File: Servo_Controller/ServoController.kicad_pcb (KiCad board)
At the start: 2 copper layers, 71.5 x 20.8 mm, 43 parts, among them J1 USB_B_Micro, K1 SWD, K2 Signal/Power, M1 Motor, U1 STM32F103C8T6, U2 TPD2E001DZDR, U3 AMS1117-3.3, U4 IRS4427S, U5 AO4616, U6 AO4616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

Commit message: Manufacturing data added
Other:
- board text added: "Servo controller"
- board text removed: "Servo controller - Variant {dblquote}A{dblquote}"
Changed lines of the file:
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@@
   (gr_line (start 304.25 191.75) (end 239.5 191.75) (layer "Edge.Cuts") (width 0.1))
   (gr_arc (start 239.5 212.5) (mid 239.146447 212.353553) (end 239 212) (layer "Edge.Cuts") (width 0.1))
-  (gr_text "Servo controller - Variant {dblquote}A{dblquote}" (at 278.3 208.25) (layer "B.SilkS")
+  (gr_text "Servo controller" (at 281.5 209.25) (layer "B.SilkS")
     (effects (font (size 1 1) (thickness 0.15)) (justify mirror))
   )

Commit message: Manual assembly PDF added, value/reference sizes changed in PCB
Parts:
- K1: value SWD -> *VAL
- renumbered R4 to Rw

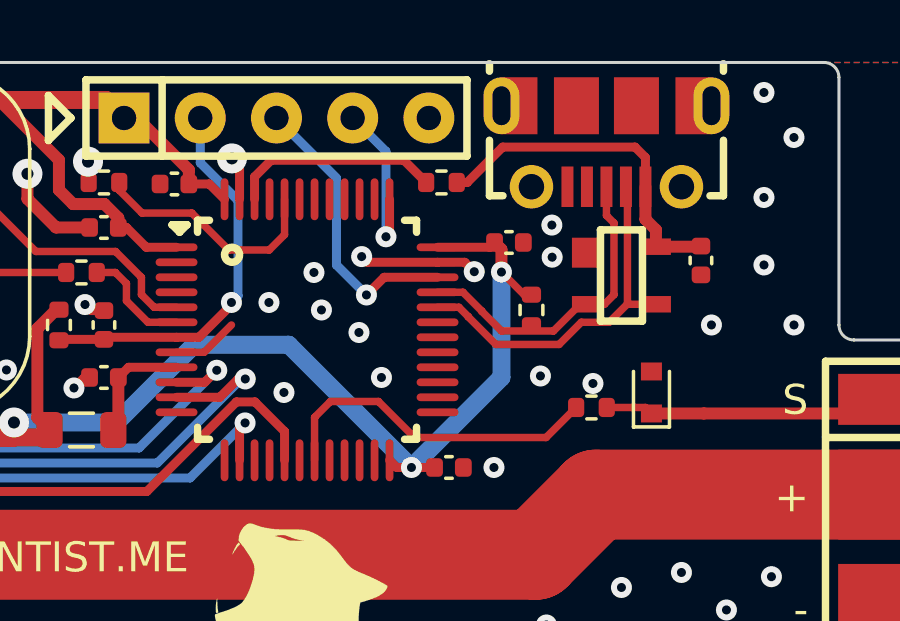
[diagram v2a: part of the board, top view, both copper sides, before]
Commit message: Added enclosure, removed unnecessary resistor
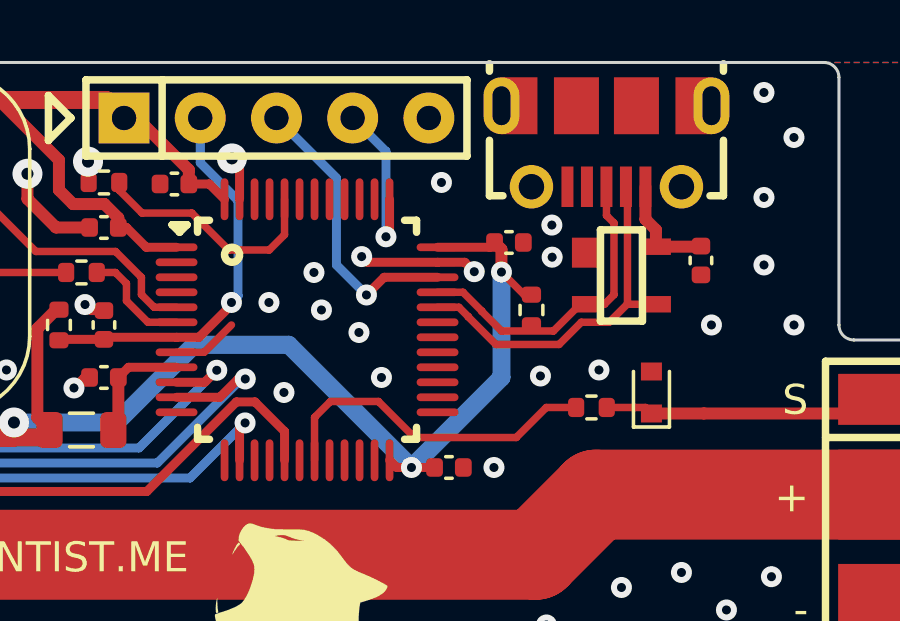
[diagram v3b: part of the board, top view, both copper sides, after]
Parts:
- removed R1: 4.7k, ServoController:R_0402
- removed Rw: 1k, ServoController:R_0402
- added R4: 1k, ServoController:R_0402, F.Cu at (296.5, 203.2)
- K1: value *VAL -> SWD
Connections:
- U1 pad 46: /USB_DET -> unconnected-(U1-Pad46)
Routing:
- net Net-(C1-Pad1): track 11.5 -> 3.65 mm
- net /USB_DET: track 7.00 -> 0.00 mm
- net GND: vias 79 -> 80

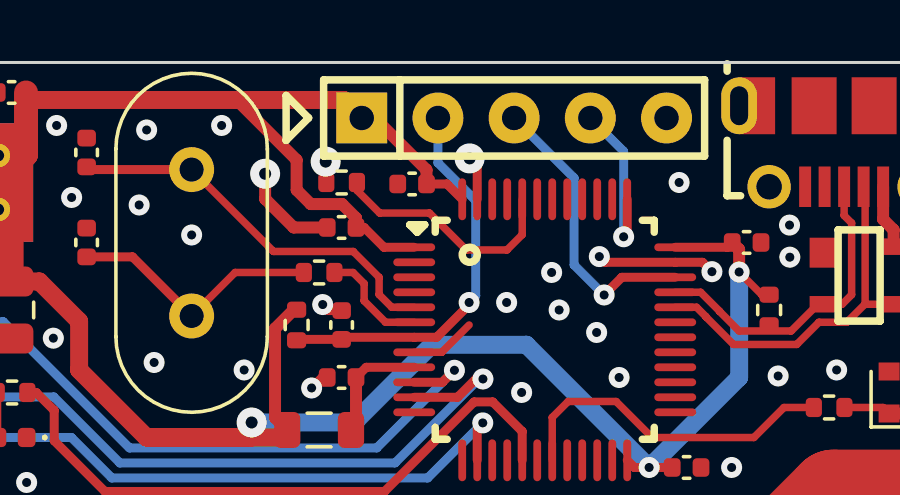
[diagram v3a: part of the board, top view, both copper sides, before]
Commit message: Changed VCC to SWO signal on SWD header. Manufacturing data and PCB previews updated
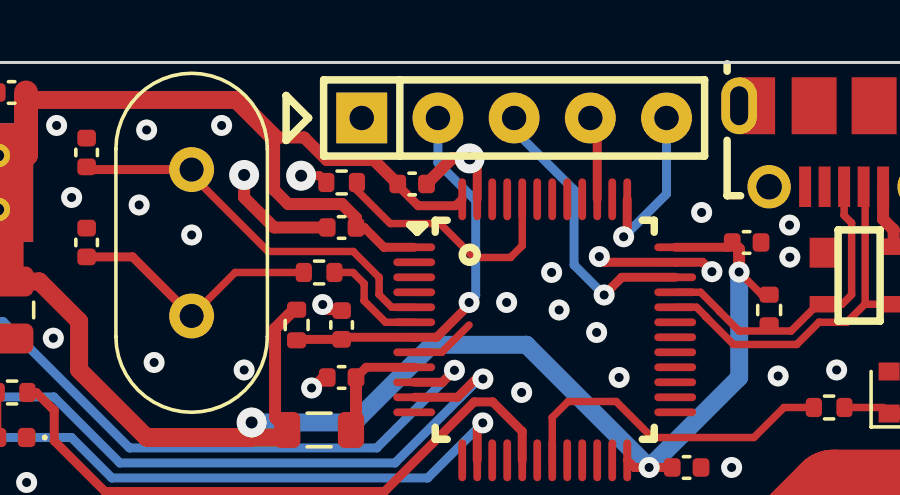
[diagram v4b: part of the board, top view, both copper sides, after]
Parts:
- turned C9 to 0 degrees
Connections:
- J1 pad 6: unconnected-(J1-Pad6) -> (no net)
- K1 pad 1: VCC -> GND
- K1 pad 4: /MCU_SWCLK -> /MCU_SWO
- K1 pad 5: GND -> /MCU_SWCLK
- U1 pad 39: unconnected-(U1-Pad39) -> /MCU_SWO
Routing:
- net /MCU_SWO: track 0.00 -> 2.81 mm
- net GND: track 13.0 -> 15.7 mm
- net VCC: track 111.0 -> 109.6 mm
